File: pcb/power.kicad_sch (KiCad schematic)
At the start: 15 parts, among them J4 Conn_01x02, Q1 Q_PMOS_DGS, SW1 POWER, U3 MCP73831-2-OT, U4 MAX17948, U6 MIC5353-3.3YMT

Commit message: pcb: Update schematic to WIP6
Change-Id: I9e9f727ad2774ee986f2f97450dc509901129aec
Reviewed-on: https://pigweed-review.googlesource.com/c/pigweed/kudzu/+/169650
Reviewed-by: Anthony DiGirolamo <tonymd@google.com>
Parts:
- added TP10 (x2): RUN, symbol Connector:TestPoint
- D2: DigiKey PN (none) -> 4786-B5819WCT-ND; Price @ 10 (none) -> 0.16400; Price @ 25 (none) -> 0.16400
- Q1: value Q_PMOS_DGS -> Q_PMOS_GSD; footprint (none) -> Package_TO_SOT_SMD:SOT-23-3; symbol Device:Q_PMOS_DGS -> Device:Q_PMOS_GSD; DigiKey PN (none) -> 31-DMG3415UQ-7CT-ND; Price @ 10 (none) -> 0.36000; Price @ 25 (none) -> 0.36000
- R6: value 1K -> 2K
- U3: DigiKey PN (none) -> MCP73831T-2ACI/MCTR-ND; Price @ 10 (none) -> 0.79000; Price @ 25 (none) -> 0.65000
- U4: value MAX17948 -> MAX17048; DigiKey PN (none) -> MAX17048G+T10TR-ND; Price @ 10 (none) -> 3.03900; Price @ 25 (none) -> 2.87280
- U6: DigiKey PN 76-3980-2-ND -> 576-3680-2-ND; Price @ 10 (none) -> 0.46000; Price @ 25 (none) -> 0.37000
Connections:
- net +BATT: now also Q1.3 (D); no longer Q1.1 (D)
- net GAUGE_ALERT_N: now also TP10.1
- net GAUGE_QSTRT: now also TP10.1
- net VBUS: now also Q1.1 (G); no longer Q1.2 (G)
- net at D2.1 (K), SW1.1 (A): now also Q1.2 (S); no longer Q1.3 (S)
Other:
- note added: "Can substitute with MIC5219-3.3YML-TR"
- note added: "Charge Current Resistor: R (KOhms) = 1000 (V) / Charge Current (mA) 2K = 500 mA (Notes 500mA may over current USB while device is running. Revisit once device power is measured.)"
- note removed: "Charge Current Resistor: R (KOhms) = 1000 (V) / Charge Current (mA) 2K = 500 mA"
- note removed: "Confirm FET pinout when part is selected"
- note removed: "Need to select LDO. This part is not in stock."
- note removed: "Need to select shottkey and FET"
- moved on the sheet: C12, C13, C14, C15, D2, J4, Q1, R6, R7, R8, R9, SW1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

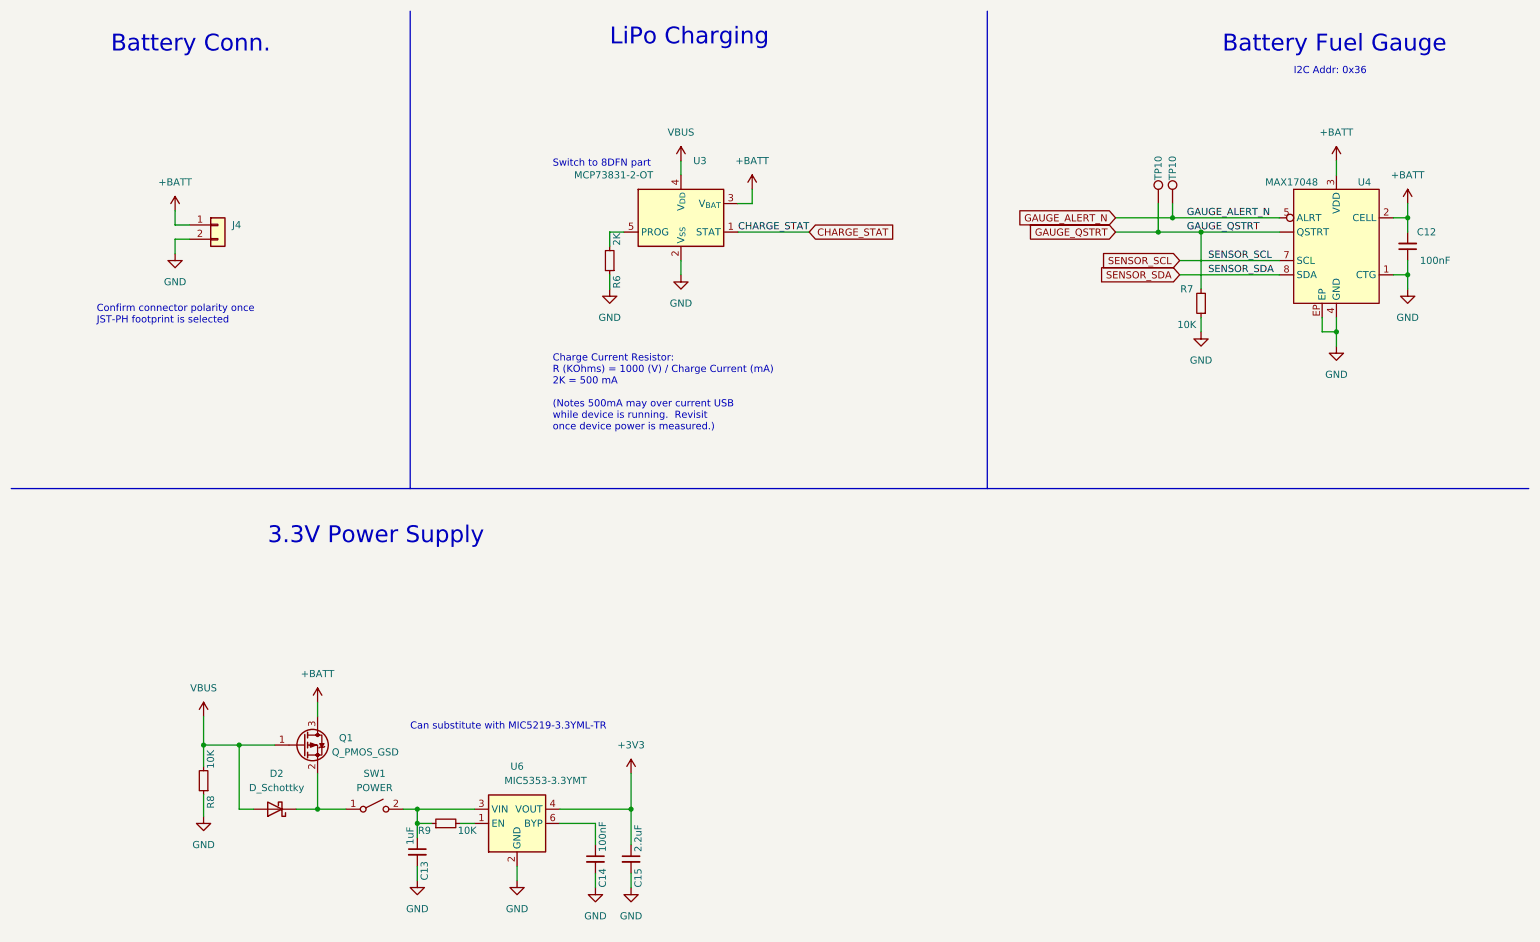
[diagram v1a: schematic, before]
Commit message: pcb: Update pcb to WIP7
Changes:

- Pruned unused parts from `kudzu-parts.kicad_sym`.
- Updated all parts in `kudzu-parts.kicad_sym` to pass `klc-check/check_symbol.py`.
- Switched to `PI4IOE5V6416` IO expander which has programmable pull-up.
- Removed pull-ups on `BOARD_ID*`, `BUTTON_*`, `TOUCH_RESET`, and `DISP_RESET`
  in favor of internal pull-ups in the IO expander.
- Added pull-up to `RESET_N`.
- Removed test points from `QSPI_*`.
- Switched to QFN version of `MCP73831`.
- Fixed missing pin number on `MAX17048` `QSTRT`.
- Removed pull-up on 3.3V regulator's `EN` pin and tied directly to `VIN`.
- Added extra decoupling caps to rp2040's 3.3V and 1.1V lines per design guide.
- Added note to add axis diagram to silk screen on board.
- Miscellaneous visual cleanup.
- Added FET on conduction path for system power.
- Added circuit to charge at 250mA when system is on and 500mA when system is off.
- Assigned all RP2040 IOs.
- Created and switched to dedicated symbols for DPAD, A/B, and SELECT/START.
- Switched display connector symbol for one with a mounting pin.
- Set test point values to net names.
- Selected LEDs and current limiting resistor values.
- Added closed solder jumpers to GBA Link signals.
- Changed solder jumper on GBA VCC pin to open.
- Changed LCD decoupling to mach reference circuit.
- Connected DISP_RD (J9 Pin 12) to +3V3.
- Connected DB0-15 (J9 Pins 17-32) to GND.
- Updated 12MHz Crystal (Y1) to correct symbol and foot print.

Change-Id: I6d0fe442c50df116031305f5165b6a29d3572d45
Reviewed-on: https://pigweed-review.googlesource.com/c/pigweed/kudzu/+/169858
Reviewed-by: Anthony DiGirolamo <tonymd@google.com>
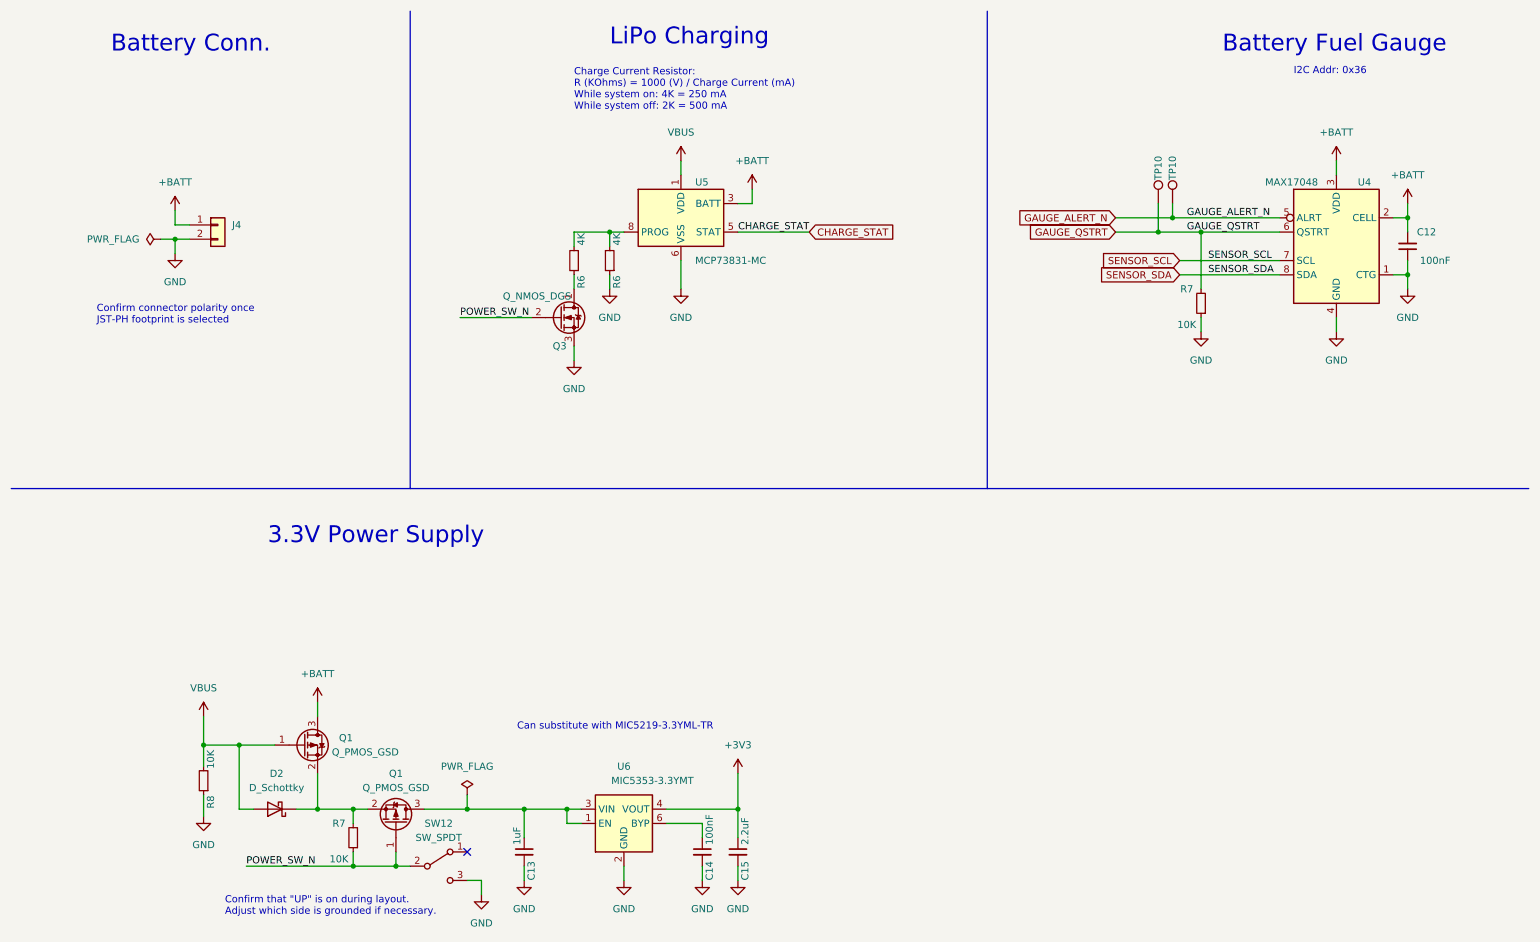
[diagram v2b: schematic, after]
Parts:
- removed R9: 10K, symbol Device:R_Small
- removed SW1: POWER, symbol Switch:SW_SPST
- removed U3: MCP73831-2-OT, Package_TO_SOT_SMD:SOT-23-5, symbol Battery_Management:MCP73831-2-OT
- added Q1: Q_PMOS_GSD, Package_TO_SOT_SMD:SOT-23-3, symbol Device:Q_PMOS_GSD
- added Q3: Q_NMOS_DGS, Package_TO_SOT_SMD:SOT-23-3, symbol Device:Q_NMOS_DGS
- added R6: 4K, Resistor_SMD:R_0603_1608Metric, symbol Device:R_Small
- added R7: 10K, Resistor_SMD:R_0603_1608Metric, symbol Device:R_Small
- added SW12: SW_SPDT, Button_Switch_SMD:SW_SPDT_CK-JS102011SAQN, symbol Switch:SW_SPDT
- added U5: MCP73831-MC, Package_DFN_QFN:DFN-8-1EP_3x2mm_P0.5mm_EP1.75x1.45mm, symbol kudzu-parts:MCP73831-MC
- C12, C13, C14, C15: footprint (none) -> Capacitor_SMD:C_0603_1608Metric
- D2: footprint (none) -> Diode_SMD:D_SOD-123
- J4: footprint (none) -> Connector_JST:JST_PH_S2B-PH-K_1x02_P2.00mm_Horizontal
- R6: value 2K -> 4K; footprint (none) -> Resistor_SMD:R_0603_1608Metric
- R7, R8: footprint (none) -> Resistor_SMD:R_0603_1608Metric
- TP10: value RUN -> GAUGE_ALERT_N; footprint (none) -> TestPoint:TestPoint_Pad_D1.0mm
- TP10: value RUN -> GAUGE_QSTRT; footprint (none) -> TestPoint:TestPoint_Pad_D1.0mm
- U4: footprint (none) -> Package_DFN_QFN:TDFN-8-1EP_2x2mm_P0.5mm_EP0.8x1.2mm
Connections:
- net +BATT: now also U5.3 (BATT), U5.4 (BATT)
- net CHARGE_STAT: now also U5.5 (STAT)
- net GAUGE_QSTRT: now also U4.6 (QSTRT); no longer U4. (QSTRT)
- net GND: now also U4.9 (GND), Q3.3 (S), SW12.3 (C), U5.6 (VSS), U5.9 (VSS); no longer U4.EP
- net VBUS: now also U5.1 (VDD), U5.2 (VDD)
- net at D2.1 (K), Q1.2 (S): now also Q1.2 (S), R7.2
- net at C13.1, U6.3 (VIN): now also U6.1 (EN), Q1.3 (D)
- net at R6.2: now also R6.2, U5.8 (PROG)
- new net: Q3.1 (D), R6.1
- new net POWER_SW_N: Q1.1 (G), Q3.2 (G), R7.1, SW12.2 (B)
- no-connect marks 0 -> 1
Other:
- note added: "Charge Current Resistor: R (KOhms) = 1000 (V) / Charge Current (mA) While system on: 4K = 250 mA While system off: 2K = 500 mA"
- note added: "Confirm that "UP" is on during layout. Adjust which side is grounded if necessary."
- note removed: "Charge Current Resistor: R (KOhms) = 1000 (V) / Charge Current (mA) 2K = 500 mA (Notes 500mA may over current USB while device is running. Revisit once device power is measured.)"
- note removed: "Switch to 8DFN part"
- moved on the sheet: C13, C14, C15, U6

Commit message: pcb: rev 0-r1 - board routed
Change-Id: Icb9c0ddbcf21cc7f2bac7bbcd371ff5a97baf35d
Reviewed-on: https://pigweed-review.googlesource.com/c/pigweed/kudzu/+/170233
Reviewed-by: Anthony DiGirolamo <tonymd@google.com>
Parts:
- J4: footprint Connector_JST:JST_PH_S2B-PH-K_1x02_P2.00mm_Horizontal -> KudzuLibrary:JST_PH_S2B-PH-SM_1x02_P2.00mm_Horizontal; DigiKey PN (none) -> 455-S2B-PH-SM4-TBCT-ND; Price @ 10 (none) -> 0.50300; Price @ 25 (none) -> 0.50300
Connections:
- net VSYS_ALWAYS: now reaches D2.1 (K), Q1.2 (S), Q1.2 (S), R7.2
- net VSYS: now reaches C13.1, Q1.3 (D), U6.1 (EN), U6.3 (VIN)
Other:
- note removed: "Confirm connector polarity once JST-PH footprint is selected"
- company: (none) -> Copyright 2023 The Pigweed Authors
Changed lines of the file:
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@@
   (title_block
     (title "Kudzu")
-    (date "2023-09-07")
-    (rev "WIP7")
+    (date "2023-09-12")
+    (rev "rev0-rc1")
+    (company "Copyright 2023 The Pigweed Authors")
   )
   (junction (at 67.31 154.94) (diameter 0) (color 0 0 0 0)
@@
     (effects (font (size 1.27 1.27)) (justify left bottom))
   )
-  (text "Confirm connector polarity once\nJST-PH footprint is selected"
-    (at 27.94 68.58 0)
-    (effects (font (size 1.27 1.27)) (justify left bottom))
-  )
   (text "LiPo Charging\n" (at 119.38 19.05 0)
     (effects (font (size 3 3)) (justify left bottom))
@@
     (effects (font (size 1.27 1.27)) (justify left bottom))
   )
+  (label "VSYS_ALWAYS" (at 66.04 154.94 0) (fields_autoplaced)
+    (effects (font (size 1.27 1.27)) (justify left bottom))
+  )
   (label "POWER_SW_N" (at 92.71 67.31 0) (fields_autoplaced)
     (effects (font (size 1.27 1.27)) (justify left bottom))
@@
   )
   (label "GAUGE_QSTRT" (at 222.25 52.07 0) (fields_autoplaced)
+    (effects (font (size 1.27 1.27)) (justify left bottom))
+  )
+  (label "VSYS" (at 97.79 154.94 0) (fields_autoplaced)
     (effects (font (size 1.27 1.27)) (justify left bottom))
   )
@@
       (effects (font (size 1.27 1.27)) (justify left) hide)
     )
-    (property "Footprint" "Connector_JST:JST_PH_S2B-PH-K_1x02_P2.00mm_Horizontal" (at 49.53 50.8 0)
+    (property "Footprint" "KudzuLibrary:JST_PH_S2B-PH-SM_1x02_P2.00mm_Horizontal" (at 49.53 50.8 0)
       (effects (font (size 1.27 1.27)) hide)
     )
@@
       (effects (font (size 1.27 1.27)) hide)
     )
-    (property "Price @ 10" "" (at 49.53 50.8 0)
-      (effects (font (size 1.27 1.27)) hide)
-    )
-    (property "Price @ 25" "" (at 49.53 50.8 0)
-      (effects (font (size 1.27 1.27)) hide)
-    )
+    (property "Price @ 10" "0.50300" (at 49.53 50.8 0)
+      (effects (font (size 1.27 1.27)) hide)
+    )
+    (property "Price @ 25" "0.50300" (at 49.53 50.8 0)
+      (effects (font (size 1.27 1.27)) hide)
+    )
+    (property "DigiKey PN" "455-S2B-PH-SM4-TBCT-ND" (at 49.53 50.8 0)
+      (effects (font (size 1.27 1.27)) hide)
+    )

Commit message: pcb: Add part numbers for passives
Change-Id: Ie1730dd2a7126b7f6f602689064a4dbf8996e7b6
Reviewed-on: https://pigweed-review.googlesource.com/c/pigweed/kudzu/+/172895
Reviewed-by: Anthony DiGirolamo <anthony.digirolamo@gmail.com>
Reviewed-by: Anthony DiGirolamo <tonymd@google.com>
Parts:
- C12, C14: DigiKey PN (none) -> 1276-1000-2-ND; Price @ 10 (none) -> 0.01200; Price @ 25 (none) -> 0.00856
- C13: DigiKey PN (none) -> 1276-1102-2-ND; Price @ 10 (none) -> 0.03100
- C15: DigiKey PN (none) -> 1276-1040-2-ND; Price @ 10 (none) -> 0.03460; Price @ 25 (none) -> 0.02830
- R6: value 4K -> 4.02K 1%; DigiKey PN (none) -> 311-4.02KHRTR-ND; Price @ 10 (none) -> 0.01800; Price @ 25 (none) -> 0.01060
- R7, R8: DigiKey PN (none) -> RNCP0603FTD10K0TR-ND; Price @ 10 (none) -> 0.03240; Price @ 25 (none) -> 0.02380
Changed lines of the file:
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@@
       (effects (font (size 1.27 1.27)) hide)
     )
-    (property "Price @ 10" "" (at 73.66 160.02 0)
-      (effects (font (size 1.27 1.27)) hide)
-    )
-    (property "Price @ 25" "" (at 73.66 160.02 0)
+    (property "Price @ 10" "0.03240" (at 73.66 160.02 0)
+      (effects (font (size 1.27 1.27)) hide)
+    )
+    (property "Price @ 25" "0.02380" (at 73.66 160.02 0)
+      (effects (font (size 1.27 1.27)) hide)
+    )
+    (property "DigiKey PN" "RNCP0603FTD10K0TR-ND" (at 73.66 160.02 0)
       (effects (font (size 1.27 1.27)) hide)
     )
@@
       (effects (font (size 1.27 1.27)))
     )
-    (property "Value" "4K" (at 120.65 53.34 90)
+    (property "Value" "4.02K 1%" (at 120.65 53.34 90)
       (effects (font (size 1.27 1.27)))
     )
@@
       (effects (font (size 1.27 1.27)) hide)
     )
-    (property "Price @ 10" "" (at 119.38 57.15 0)
-      (effects (font (size 1.27 1.27)) hide)
-    )
-    (property "Price @ 25" "" (at 119.38 57.15 0)
+    (property "Price @ 10" "0.01800" (at 119.38 57.15 0)
+      (effects (font (size 1.27 1.27)) hide)
+    )
+    (property "Price @ 25" "0.01060" (at 119.38 57.15 0)
+      (effects (font (size 1.27 1.27)) hide)
+    )
+    (property "DigiKey PN" "311-4.02KHRTR-ND" (at 119.38 57.15 0)
       (effects (font (size 1.27 1.27)) hide)
     )
@@
       (effects (font (size 1.27 1.27)) hide)
     )
-    (property "Price @ 10" "" (at 46.99 149.86 0)
-      (effects (font (size 1.27 1.27)) hide)
-    )
-    (property "Price @ 25" "" (at 46.99 149.86 0)
+    (property "Price @ 10" "0.03240" (at 46.99 149.86 0)
+      (effects (font (size 1.27 1.27)) hide)
+    )
+    (property "Price @ 25" "0.02380" (at 46.99 149.86 0)
+      (effects (font (size 1.27 1.27)) hide)
+    )
+    (property "DigiKey PN" "RNCP0603FTD10K0TR-ND" (at 46.99 149.86 0)
       (effects (font (size 1.27 1.27)) hide)
     )
@@
       (effects (font (size 1.27 1.27)) hide)
     )
-    (property "Price @ 10" "" (at 104.14 162.56 0)
+    (property "Price @ 10" "0.03100" (at 104.14 162.56 0)
       (effects (font (size 1.27 1.27)) hide)
     )
     (property "Price @ 25" "" (at 104.14 162.56 0)
+      (effects (font (size 1.27 1.27)) hide)
+    )
+    (property "DigiKey PN" "1276-1102-2-ND" (at 104.14 162.56 0)
       (effects (font (size 1.27 1.27)) hide)
     )
@@
       (effects (font (size 1.27 1.27)) hide)
     )
-    (property "Price @ 10" "" (at 224.79 64.77 0)
-      (effects (font (size 1.27 1.27)) hide)
-    )
-    (property "Price @ 25" "" (at 224.79 64.77 0)
+    (property "Price @ 10" "0.03240" (at 224.79 64.77 0)
+      (effects (font (size 1.27 1.27)) hide)
+    )
+    (property "Price @ 25" "0.02380" (at 224.79 64.77 0)
+      (effects (font (size 1.27 1.27)) hide)
+    )
+    (property "DigiKey PN" "RNCP0603FTD10K0TR-ND" (at 224.79 64.77 0)
       (effects (font (size 1.27 1.27)) hide)
     )
@@
       (effects (font (size 1.27 1.27)))
     )
-    (property "Value" "4K" (at 114.3 53.34 90)
+    (property "Value" "4.02K 1%" (at 114.3 53.34 90)
       (effects (font (size 1.27 1.27)))
     )
@@
       (effects (font (size 1.27 1.27)) hide)
     )
-    (property "Price @ 10" "" (at 113.03 57.15 0)
-      (effects (font (size 1.27 1.27)) hide)
-    )
-    (property "Price @ 25" "" (at 113.03 57.15 0)
+    (property "Price @ 10" "0.01800" (at 113.03 57.15 0)
+      (effects (font (size 1.27 1.27)) hide)
+    )
+    (property "Price @ 25" "0.01060" (at 113.03 57.15 0)
+      (effects (font (size 1.27 1.27)) hide)
+    )
+    (property "DigiKey PN" "311-4.02KHRTR-ND" (at 113.03 57.15 0)
       (effects (font (size 1.27 1.27)) hide)
     )
@@
       (effects (font (size 1.27 1.27)) hide)
     )
-    (property "Price @ 10" "" (at 142.24 162.56 0)
-      (effects (font (size 1.27 1.27)) hide)
-    )
-    (property "Price @ 25" "" (at 142.24 162.56 0)
+    (property "Price @ 10" "0.03460" (at 142.24 162.56 0)
+      (effects (font (size 1.27 1.27)) hide)
+    )
+    (property "Price @ 25" "0.02830" (at 142.24 162.56 0)
+      (effects (font (size 1.27 1.27)) hide)
+    )
+    (property "DigiKey PN" "1276-1040-2-ND" (at 142.24 162.56 0)
       (effects (font (size 1.27 1.27)) hide)
     )
@@
       (effects (font (size 1.27 1.27)) hide)
     )
-    (property "Price @ 10" "" (at 261.62 54.61 0)
-      (effects (font (size 1.27 1.27)) hide)
-    )
-    (property "Price @ 25" "" (at 261.62 54.61 0)
+    (property "Price @ 10" "0.01200" (at 261.62 54.61 0)
+      (effects (font (size 1.27 1.27)) hide)
+    )
+    (property "Price @ 25" "0.00856" (at 261.62 54.61 0)
+      (effects (font (size 1.27 1.27)) hide)
+    )
+    (property "DigiKey PN" "1276-1000-2-ND" (at 261.62 54.61 0)
       (effects (font (size 1.27 1.27)) hide)
     )
@@
       (effects (font (size 1.27 1.27)) hide)
     )
-    (property "Price @ 10" "" (at 135.89 162.56 0)
-      (effects (font (size 1.27 1.27)) hide)
-    )
-    (property "Price @ 25" "" (at 135.89 162.56 0)
-      (effects (font (size 1.27 1.27)) hide)
-    )
+    (property "Price @ 10" "0.01200" (at 135.89 162.56 0)
+      (effects (font (size 1.27 1.27)) hide)
+    )
+    (property "Price @ 25" "0.00856" (at 135.89 162.56 0)
+      (effects (font (size 1.27 1.27)) hide)
+    )
+    (property "DigiKey PN" "1276-1000-2-ND" (at 135.89 162.56 0)
+      (effects (font (size 1.27 1.27)) hide)
+    )

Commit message: pcb: Use GSD pinout for Q3
Part and pinout did not match in Rev 0.

Change-Id: Ia9c9112f3c1dfc869c1e90e9dbf6ccad72d5fb3f
Reviewed-on: https://pigweed-review.googlesource.com/c/pigweed/kudzu/+/172970
Reviewed-by: Anthony DiGirolamo <anthony.digirolamo@gmail.com>
Reviewed-by: Anthony DiGirolamo <tonymd@google.com>
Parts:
- Q3: value Q_NMOS_DGS -> Q_NMOS_GSD; symbol Device:Q_NMOS_DGS -> Device:Q_NMOS_GSD
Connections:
- net GND: now also Q3.2 (S); no longer Q3.3 (S)
- net POWER_SW_N: now also Q3.1 (G); no longer Q3.2 (G)
- net at R6.1: now also Q3.3 (D); no longer Q3.1 (D)
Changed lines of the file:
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@@
     )
   )
-  (symbol (lib_id "Device:Q_NMOS_DGS") (at 110.49 67.31 0) (unit 1)
+  (symbol (lib_id "Device:Q_NMOS_GSD") (at 110.49 67.31 0) (unit 1)
     (in_bom yes) (on_board yes) (dnp no)
     (property "Reference" "Q3" (at 109.22 72.39 0)
       (effects (font (size 1.27 1.27)) (justify left))
     )
-    (property "Value" "Q_NMOS_DGS" (at 100.33 63.5 0)
+    (property "Value" "Q_NMOS_GSD" (at 100.33 63.5 0)
       (effects (font (size 1.27 1.27)) (justify left))
     )
